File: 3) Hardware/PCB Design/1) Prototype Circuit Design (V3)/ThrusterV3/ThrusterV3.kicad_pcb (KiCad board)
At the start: 2 copper layers, 90 x 90 mm, 68 parts, among them J8 USB_C_Receptacle, Q1 AO3400A, Q2 AO3400A, Q3 AO3400A, Q4 AO3400A, Q5 AO3400A, Q6 IPD70P04P4L08ATMA2, SW1 SW_Push, U1 INA126U, U2 STM32G491CCTx, U3 AP63205WU, U4 AMS1117-3.3, U5 ADS131M04IPWR, Y1 8MHz

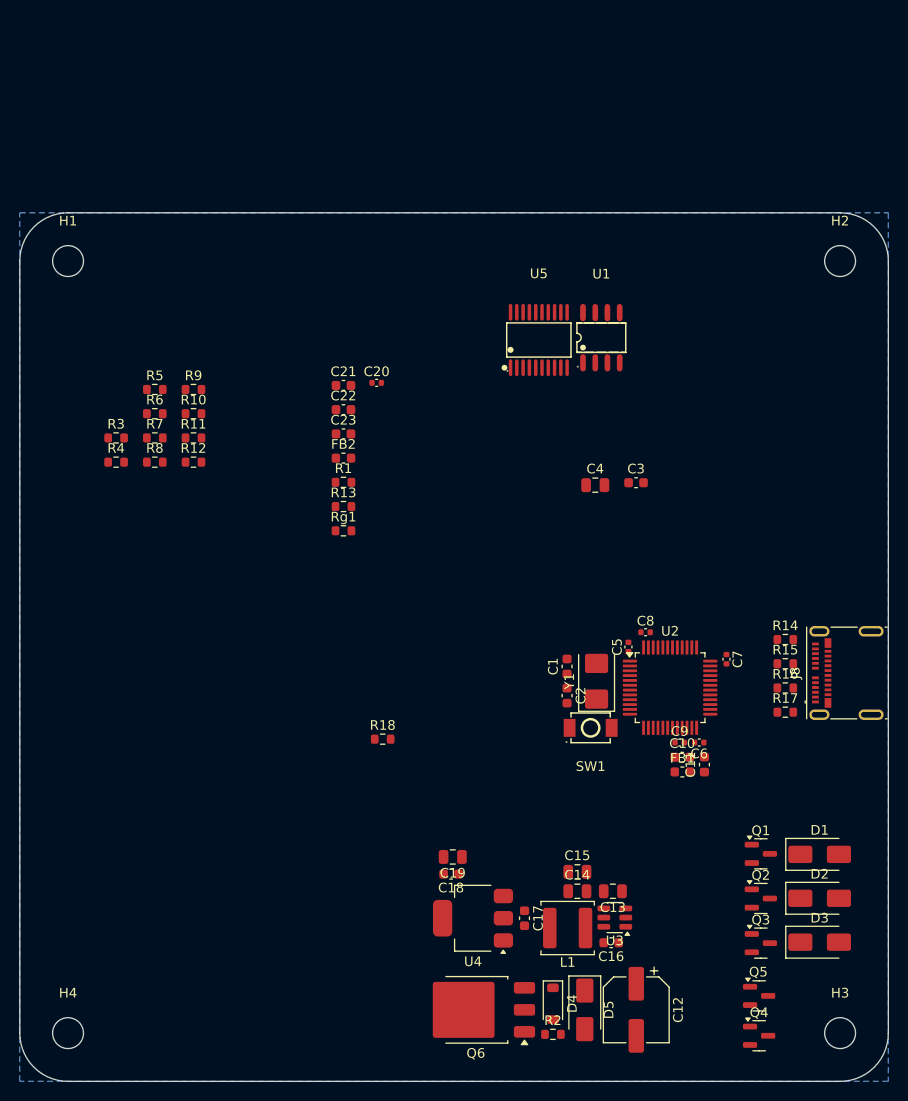
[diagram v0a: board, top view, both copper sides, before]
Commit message: Finished Routing Thruster V3 PCB
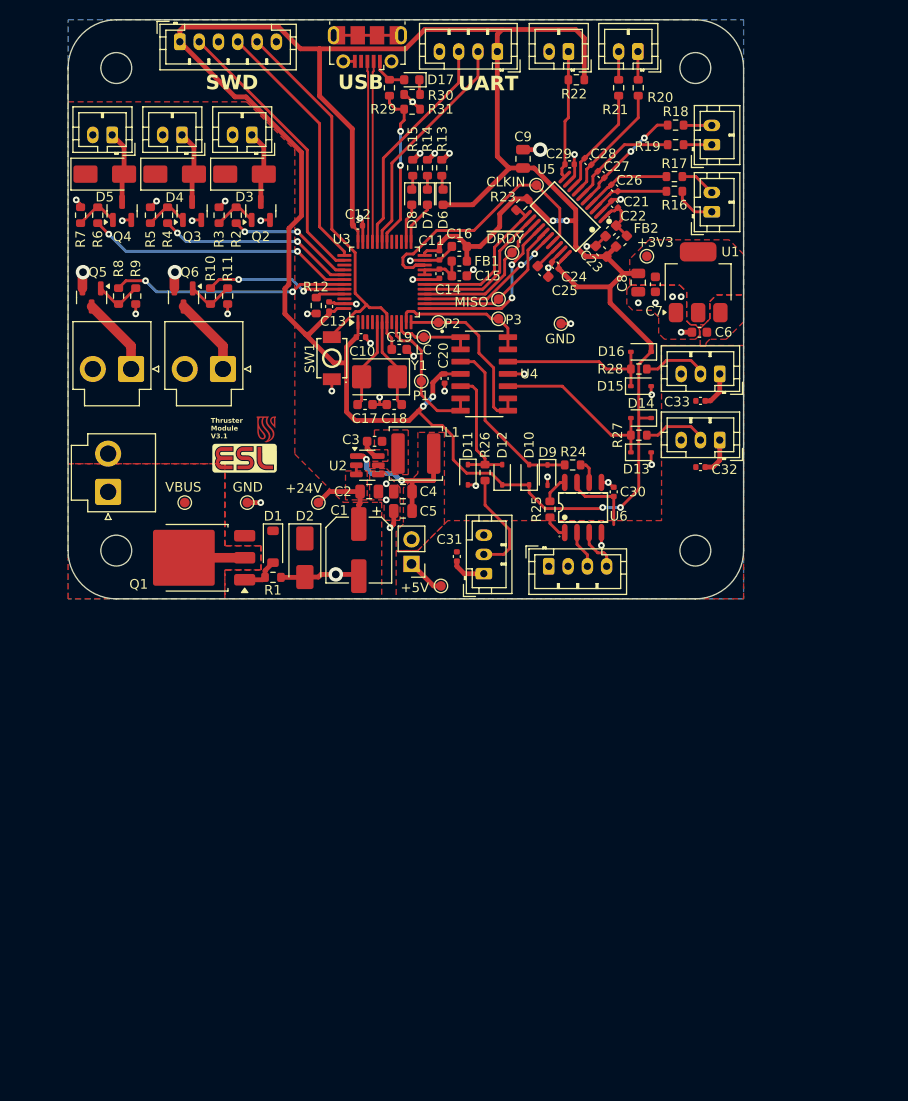
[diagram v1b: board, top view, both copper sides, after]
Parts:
- removed the C3 at (163.9, 103.0)
- removed the C4 at (159.6, 103.2)
- removed the D1 at (182.9, 141.5)
- removed the D2 at (182.9, 146.0)
- removed the Q1 at (176.8, 141.4)
- removed the R1 at (133.5, 102.9)
- removed Rg1: R, Resistor_SMD:R_0603_1608Metric
- removed the U1 at (160.3, 87.9)
- added C19: 100n, Capacitor_SMD:C_0603_1608Metric, F.Cu at (139.3, 89.2)
- added C24: 100n, Capacitor_SMD:C_0402_1005Metric, F.Cu at (155.5, 80.4)
- added C25: 220n, Capacitor_SMD:C_0603_1608Metric, F.Cu at (154.2, 81.1)
- added C26: 10n, Capacitor_SMD:C_0402_1005Metric, F.Cu at (161.6, 72.4)
- added C27: 10n, Capacitor_SMD:C_0402_1005Metric, F.Cu at (160.2, 71.0)
- added C28: 10n, Capacitor_SMD:C_0402_1005Metric, F.Cu at (158.9, 69.7)
- added C29: 10n, Capacitor_SMD:C_0402_1005Metric, F.Cu at (157.0, 70.0)
- added C30: 100n, Capacitor_SMD:C_0402_1005Metric, F.Cu at (161.5, 103.9)
- added C31: 100n, Capacitor_SMD:C_0402_1005Metric, F.Cu at (145.3, 110.6)
- added C32: 100n, Capacitor_SMD:C_0402_1005Metric, F.Cu at (170.5, 101.3)
- added C33: 100n, Capacitor_SMD:C_0402_1005Metric, F.Cu at (170.5, 94.5)
- added C9: 10u, Capacitor_SMD:C_0805_2012Metric, F.Cu at (152.1, 69.4)
- added D10: 1N5819WS, Diode_SMD:D_SOD-323, F.Cu at (152.8, 102.1)
- added D11: 1N5819WS, Diode_SMD:D_SOD-323, F.Cu at (146.4, 102.1)
- added D12: 1N5819WS, Diode_SMD:D_SOD-323, F.Cu at (150.0, 102.1)
- added D13: 1N5819WS, Diode_SMD:D_SOD-323, F.Cu at (164.4, 99.8)
- added D14: 1N5819WS, Diode_SMD:D_SOD-323, F.Cu at (164.4, 96.3)
- added D15: 1N5819WS, Diode_SMD:D_SOD-323, F.Cu at (164.4, 93.0)
- added D16: 1N5819WS, Diode_SMD:D_SOD-323, F.Cu at (164.4, 89.4)
- added D17: LED, LED_SMD:LED_0603_1608Metric, F.Cu at (140.6, 61.2)
- added D4: SS14, Diode_SMD:D_SMA, F.Cu at (116.0, 71.0)
- added D5: SS14, Diode_SMD:D_SMA, F.Cu at (108.8, 71.0)
- added D6: LED, LED_SMD:LED_0603_1608Metric, F.Cu at (143.9, 73.4)
- added D7: LED, LED_SMD:LED_0603_1608Metric, F.Cu at (142.2, 73.4)
- added D8: LED, LED_SMD:LED_0603_1608Metric, F.Cu at (140.6, 73.4)
- added D9: 1N5819WS, Diode_SMD:D_SOD-323, F.Cu at (154.7, 102.2)
- added ESL_LOGO, G***: LOGO, LOGO, F.Cu at (123.3, 100.4)
- added J1: Conn_01x02_Pin, Connector_JST:JST_VH_B2P-VH_1x02_P3.96mm_Vertical, F.Cu at (109.2, 103.9)
- added J10: Conn_01x02_Pin, Connector_JST:JST_PH_B2B-PH-K_1x02_P2.00mm_Vertical, F.Cu at (164.1, 58.3)
- added J11: Conn_01x02_Pin, Connector_JST:JST_PH_B2B-PH-K_1x02_P2.00mm_Vertical, F.Cu at (156.8, 58.3)
- added J12: Conn_01x04_Pin, Connector_JST:JST_PH_B4B-PH-K_1x04_P2.00mm_Vertical, F.Cu at (154.8, 111.6)
- added J13: Conn_01x03_Pin, Connector_JST:JST_PH_B3B-PH-K_1x03_P2.00mm_Vertical, F.Cu at (148.1, 112.4)
- added J14: Conn_01x03_Pin, Connector_JST:JST_PH_B3B-PH-K_1x03_P2.00mm_Vertical, F.Cu at (172.5, 98.6)
- added J15: Conn_01x03_Pin, Connector_JST:JST_PH_B3B-PH-K_1x03_P2.00mm_Vertical, F.Cu at (172.5, 91.7)
- added J16: Conn_01x04_Pin, Connector_JST:JST_PH_B4B-PH-K_1x04_P2.00mm_Vertical, F.Cu at (149.5, 58.3)
- added J17: USB_B_Micro, Connector_USB:USB_Micro-B_Molex-105017-0001, F.Cu at (136.0, 57.8)
- added J18: SWD, Connector_JST:JST_PH_B6B-PH-K_1x06_P2.00mm_Vertical, F.Cu at (116.6, 57.3)
- added J2: Conn_01x02_Pin, Connector_PinHeader_2.54mm:PinHeader_1x02_P2.54mm_Vertical, F.Cu at (140.6, 111.4)
- added J3: Conn_01x02_Pin, Connector_JST:JST_PH_B2B-PH-K_1x02_P2.00mm_Vertical, F.Cu at (124.0, 66.9)
- added J4: Conn_01x02_Pin, Connector_JST:JST_PH_B2B-PH-K_1x02_P2.00mm_Vertical, F.Cu at (116.8, 66.9)
- added J5: Conn_01x02_Pin, Connector_JST:JST_PH_B2B-PH-K_1x02_P2.00mm_Vertical, F.Cu at (109.6, 66.9)
- added J6: Conn_01x02_Pin, Connector_JST:JST_VH_B2P-VH_1x02_P3.96mm_Vertical, F.Cu at (111.5, 91.2)
- added J7: Conn_01x02_Pin, Connector_JST:JST_VH_B2P-VH_1x02_P3.96mm_Vertical, F.Cu at (121.1, 91.2)
- added J9: Conn_01x02_Pin, Connector_JST:JST_PH_B2B-PH-K_1x02_P2.00mm_Vertical, F.Cu at (171.7, 67.9)
- added Q6: AO3400A, Package_TO_SOT_SMD:SOT-23, F.Cu at (117.0, 83.8)
- added R19: 100, Resistor_SMD:R_0603_1608Metric, F.Cu at (168.0, 67.9)
- added R2: 100, Resistor_SMD:R_0603_1608Metric, F.Cu at (122.4, 75.2)
- added R20: 100, Resistor_SMD:R_0603_1608Metric, F.Cu at (164.1, 62.0)
- added R21: 100, Resistor_SMD:R_0603_1608Metric, F.Cu at (162.1, 62.0)
- added R22: 10k, Resistor_SMD:R_0603_1608Metric, F.Cu at (157.7, 61.2)
- added R23: 10k, Resistor_SMD:R_0603_1608Metric, F.Cu at (152.0, 74.1)
- added R24: 100, Resistor_SMD:R_0603_1608Metric, F.Cu at (157.3, 101.1)
- added R25: R, Resistor_SMD:R_0603_1608Metric, F.Cu at (154.9, 105.7)
- added R26: 330, Resistor_SMD:R_0603_1608Metric, F.Cu at (148.2, 101.9)
- added R27: 330, Resistor_SMD:R_0603_1608Metric, F.Cu at (164.1, 98.0)
- added R28: 330, Resistor_SMD:R_0603_1608Metric, F.Cu at (164.1, 91.2)
- added R29: 68k, Resistor_SMD:R_0603_1608Metric, F.Cu at (138.3, 62.0)
- added R30: 100k, Resistor_SMD:R_0603_1608Metric, F.Cu at (140.7, 64.3)
- added R31: 1k, Resistor_SMD:R_0603_1608Metric, F.Cu at (140.7, 62.7)
- added SU_LOGO: LOGO, LOGO, F.Cu at (125.5, 97.4)
- added TP1: TestPoint, TestPoint:TestPoint_Pad_D1.0mm, F.Cu at (117.1, 105.0)
- added TP10: TestPoint, TestPoint:TestPoint_Pad_D1.0mm, F.Cu at (149.6, 83.9)
- added TP11: TestPoint, TestPoint:TestPoint_Pad_D1.0mm, F.Cu at (156.1, 86.5)
- added TP12: TestPoint, TestPoint:TestPoint_Pad_D1.0mm, F.Cu at (151.0, 79.1)
- added TP13: TestPoint, TestPoint:TestPoint_Pad_D1.0mm, F.Cu at (153.5, 72.1)
- added TP2: TestPoint, TestPoint:TestPoint_Pad_D1.0mm, F.Cu at (149.6, 86.0)
- added TP3: TestPoint, TestPoint:TestPoint_Pad_D1.0mm, F.Cu at (130.9, 105.0)
- added TP4: TestPoint, TestPoint:TestPoint_Pad_D1.0mm, F.Cu at (143.4, 86.4)
- added TP5: TestPoint, TestPoint:TestPoint_Pad_D1.0mm, F.Cu at (143.6, 113.7)
- added TP6: TestPoint, TestPoint:TestPoint_Pad_D1.0mm, F.Cu at (141.6, 92.5)
- added TP7: TestPoint, TestPoint:TestPoint_Pad_D1.0mm, F.Cu at (165.0, 79.5)
- added TP8: TestPoint, TestPoint:TestPoint_Pad_D1.0mm, F.Cu at (141.9, 87.9)
- added TP9: TestPoint, TestPoint:TestPoint_Pad_D1.0mm, F.Cu at (123.6, 105.0)
- added U4: MCP6024-E_SL, ESLThrusterParts:SOIC127P600X175-14N, F.Cu at (148.1, 91.7)
- added U6: INA126U, ESLThrusterParts:SOIC-8_L4.9-W3.9-P1.27-LS6.0-BL, F.Cu at (158.4, 105.5)
- C20: value 10n -> 100n
- C21: value 1u -> 10n; footprint Capacitor_SMD:C_0603_1608Metric -> Capacitor_SMD:C_0402_1005Metric
- C23: value 220n -> 1u
- J8: value USB_C_Receptacle -> Conn_01x02_Pin; footprint Connector_USB:USB_C_Receptacle_Molex_105450-0101 -> Connector_JST:JST_PH_B2B-PH-K_1x02_P2.00mm_Vertical
- R10, R18, R4, R6, R8: value 10k -> 100
- R11, R3, R5, R7, R9: value 100 -> 10k
- R13: value 10k -> 680R
- R14, R15: value 5.1k -> 680R
- R16: value 68k -> 100
- R17: value 100k -> 100
- SW1: footprint easyeda2kicad:SW-SMD_L3.9-W3.0-P4.45 -> ESLThrusterParts:SW-SMD_L3.9-W3.0-P4.45
- U5: footprint easyeda2kicad:TSSOP-20_L6.5-W4.4-P0.65-LS6.4-BL -> ESLThrusterParts:TSSOP-20_L6.5-W4.4-P0.65-LS6.4-BL
- moved Q4 108.0 mm to (110.6, 74.8), turned to 90 degrees
- moved Q5 100.1 mm to (107.4, 83.8), turned to -90 degrees
- moved D3 99.4 mm to (123.3, 71.0)
- moved Q3 96.1 mm to (117.9, 74.8), turned to 90 degrees
- moved Q2 88.1 mm to (125.0, 74.8), turned to 90 degrees
- moved R18 70.5 mm to (168.0, 65.9), turned to 180 degrees
- moved U1 69.9 mm to (170.3, 82.2), turned to 90 degrees
- moved C7 64.7 mm to (165.9, 82.4), turned to 90 degrees
- moved R15 64.3 mm to (140.7, 70.3), turned to 90 degrees
- moved C6 63.4 mm to (170.4, 87.4), turned to 180 degrees
- moved C8 62.5 mm to (164.1, 82.2), turned to 90 degrees
- moved R14 61.4 mm to (142.2, 70.3), turned to 90 degrees
- moved C16 59.4 mm to (145.5, 78.5), turned to 180 degrees
- moved C12 59.0 mm to (135.0, 76.3), turned to 0 degrees
- moved FB1 57.8 mm to (145.5, 80.0)
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- renumbered C12 to C1, C5 to C10, C6 to C11, C7 to C12, C8 to C13, C9 to C14, C10 to C15, C11 to C16, C1 to C17, C2 to C18, C13 to C2, C16 to C3, C14 to C4, C15 to C5, C17 to C6, C18 to C7, C19 to C8, D4 to D1, D5 to D2, Q6 to Q1, R2 to R1, U4 to U1, U3 to U2, U2 to U3
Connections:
- C20 pad 1: VDDA -> +3.3V
- C22 pad 1: +3.3V -> VDDA
- C23 pad 1: GND -> +3.3V
- C23 pad 2: Net-(U5-CAP) -> GND
- C4 pad 1: +5V -> Net-(J2-Pin_2)
- C5 pad 1: +5V -> Net-(J2-Pin_2)
- L1 pad 2: +5V -> Net-(J2-Pin_2)
- Q2 pad 3: Net-(D2-A) -> Net-(D3-A)
- Q3 pad 3: Net-(D3-A) -> Net-(D4-A)
- R10 pad 1: Net-(Q4-G) -> Net-(Q6-G)
- R10 pad 2: GND -> GPIO5_Heater
- R11 pad 1: Net-(Q5-G) -> Net-(Q6-G)
- R11 pad 2: GPIO5_Heater -> GND
- R12 pad 1: Net-(Q5-G) -> Net-(U3-PB8)
- R13 pad 1: +3.3V -> Net-(D6-K)
- R13 pad 2: ADC_~{SYNC}/~{RESET} -> GND
- R14 pad 1: Net-(J8-CC1) -> Net-(D7-K)
- R15 pad 1: Net-(J8-CC2) -> Net-(D8-K)
- R16 pad 1: Net-(J8-VBUS-PadA4) -> Net-(J8-Pin_1)
- R16 pad 2: VBUS_SENSING -> Net-(U5-AIN0P)
- R17 pad 1: VBUS_SENSING -> Net-(J8-Pin_2)
- R17 pad 2: GND -> Net-(U5-AIN0N)
- R18 pad 1: Net-(U2-PB8) -> Net-(J9-Pin_2)
- R18 pad 2: GND -> Net-(U5-AIN1N)
- R3 pad 1: Net-(Q1-G) -> Net-(Q2-G)
- R3 pad 2: GPIO1_Valve -> GND
- R4 pad 1: Net-(Q1-G) -> Net-(Q3-G)
- R4 pad 2: GND -> GPIO2_Valve
- R5 pad 1: Net-(Q2-G) -> Net-(Q3-G)
- R5 pad 2: GPIO2_Valve -> GND
- R6 pad 1: Net-(Q2-G) -> Net-(Q4-G)
- R6 pad 2: GND -> GPIO3_Valve
- R7 pad 1: Net-(Q3-G) -> Net-(Q4-G)
- R7 pad 2: GPIO3_Valve -> GND
- R8 pad 1: Net-(Q3-G) -> Net-(Q5-G)
- R8 pad 2: GND -> GPIO4_Heater
- R9 pad 1: Net-(Q4-G) -> Net-(Q5-G)
- R9 pad 2: GPIO4_Heater -> GND
- U2 pad 1: +5V -> Net-(J2-Pin_2)
- U3 pad 10: unconnected-(U2-PA2-Pad10) -> ADC_LOADCELL
- U3 pad 11: unconnected-(U2-PA3-Pad11) -> ADC_PRESSURE3
- U3 pad 12: unconnected-(U2-PA4-Pad12) -> ADC_PRESSURE2
- U3 pad 13: unconnected-(U2-PA5-Pad13) -> ADC_SCLK
- U3 pad 14: unconnected-(U2-PA6-Pad14) -> ADC_MISO
- U3 pad 15: unconnected-(U2-PA7-Pad15) -> ADC_MOSI
- U3 pad 16: unconnected-(U2-PB0-Pad16) -> ADC_~{DRDY}
- U3 pad 17: unconnected-(U2-PB1-Pad17) -> ADC_~{CS}
- U3 pad 18: unconnected-(U2-PB2-Pad18) -> ADC_~{SYNC}/~{RESET}
- U3 pad 22: unconnected-(U2-PB10-Pad22) -> ADC_CLKIN
- U3 pad 25: unconnected-(U2-PB11-Pad25) -> DEBUG_1
- U3 pad 26: unconnected-(U2-PB12-Pad26) -> DEBUG_2
- U3 pad 30: unconnected-(U2-PA8-Pad30) -> USB_SENSING
- U3 pad 31: unconnected-(U2-PA9-Pad31) -> UART_TX
- U3 pad 32: unconnected-(U2-PA10-Pad32) -> UART_RX
- U3 pad 33: USB_DM -> USB_DN
- U3 pad 40: SWO -> GPIO1_Valve
- U3 pad 41: unconnected-(U2-PB4-Pad41) -> GPIO2_Valve
- U3 pad 42: unconnected-(U2-PB5-Pad42) -> GPIO3_Valve
- U3 pad 43: unconnected-(U2-PB6-Pad43) -> GPIO4_Heater
- U3 pad 44: unconnected-(U2-PB7-Pad44) -> GPIO5_Heater
- U3 pad 45: Net-(U2-PB8) -> Net-(U3-PB8)
- U3 pad 9: unconnected-(U2-PA1-Pad9) -> ADC_PRESSURE1
- U5 pad 10: unconnected-(U5-AIN3P-Pad10) -> Net-(J11-Pin_1)
- U5 pad 3: unconnected-(U5-AIN0P-Pad3) -> Net-(U5-AIN0P)
- U5 pad 4: unconnected-(U5-AIN0N-Pad4) -> Net-(U5-AIN0N)
- U5 pad 5: unconnected-(U5-AIN1N-Pad5) -> Net-(U5-AIN1N)
- U5 pad 6: unconnected-(U5-AIN1P-Pad6) -> Net-(U5-AIN1P)
- U5 pad 7: unconnected-(U5-AIN2P-Pad7) -> Net-(U5-AIN2P)
- U5 pad 8: unconnected-(U5-AIN2N-Pad8) -> Net-(U5-AIN2N)
- U5 pad 9: unconnected-(U5-AIN3N-Pad9) -> GND
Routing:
- net +3.3V: track 0.00 -> 276.6 mm, vias 0 -> 6
- net GND: track 0.00 -> 91.5 mm, vias 0 -> 48
- net NRST: track 0.00 -> 43.3 mm
- net SWCLK: track 0.00 -> 29.4 mm
- net ADC_CLKIN: track 0.00 -> 28.5 mm
- net GPIO3_Valve: track 0.00 -> 28.0 mm, vias 0 -> 2
- net SWDIO: track 0.00 -> 26.7 mm
- net GPIO4_Heater: track 0.00 -> 24.5 mm, vias 0 -> 2
- net UART_TX: track 0.00 -> 23.8 mm
- net UART_RX: track 0.00 -> 23.2 mm
- net GPIO2_Valve: track 0.00 -> 20.5 mm, vias 0 -> 2
- net USB_DP: track 0.00 -> 18.7 mm
- net USB_DN: track 0.00 -> 18.7 mm
- net ADC_PRESSURE2: track 0.00 -> 18.5 mm
- net S_OUT2: track 0.00 -> 18.4 mm
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- added copper zone on F.Cu, net +24V
- added copper zone on F.Cu, net +3.3V
- added copper zone on F.Cu, net +5V
- added copper zone on F.Cu, net GND
- added copper zone on F.Cu, net Net-(J2-Pin_2)
- added copper zone on F.Cu, net Net-(U2-SW)
- added copper zone on F.Cu, net VBUS
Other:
- board size 90 x 90 mm -> 70 x 60 mm
- board text added: "+24V"
- board text added: "+3V3"
- board text added: "+5V"
- board text added: "CLKIN"
- board text added: "GND"
- board text added: "LC"
- board text added: "MISO"
- board text added: "P1"
- board text added: "P2"
- board text added: "P3"
- board text added: "SWD"
- board text added: "Thruster Module V3.1"
- board text added: "UART"
- board text added: "USB"
- board text added: "VBUS"
- board text added: "~{DRDY}"
